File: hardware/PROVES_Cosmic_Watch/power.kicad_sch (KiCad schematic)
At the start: 19 parts, among them J1 USB_B_Micro, J4 Conn_Coaxial, U3 LT3461ES6-TRPBF

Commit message: Updates
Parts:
- removed FB1: 2.5kohm, symbol Device:FerriteBead
- removed J4: Conn_Coaxial, symbol Connector:Conn_Coaxial
- added J2: Conn_01x02, symbol Connector_Generic:Conn_01x02
- added L2: BLM18BD252SN1D, BLM18BD252SN1D:L0603, symbol BLM18BD252SN1D:BLM18BD252SN1D
- J1: footprint (none) -> MOLEX MicroUSB:MICRO-USB-SMD_5P-P0.65-H-F_105164-0001
- U2: renamed from U3; footprint (none) -> LT3461:TSOT-23_S6_LIT
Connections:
- net V_Bias: now also L2.1
- net V_Out: now also L2.2
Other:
- note added: "Power from Payload Computer"
- note removed: "From the Payload Computer"
- note removed: "LT3461"

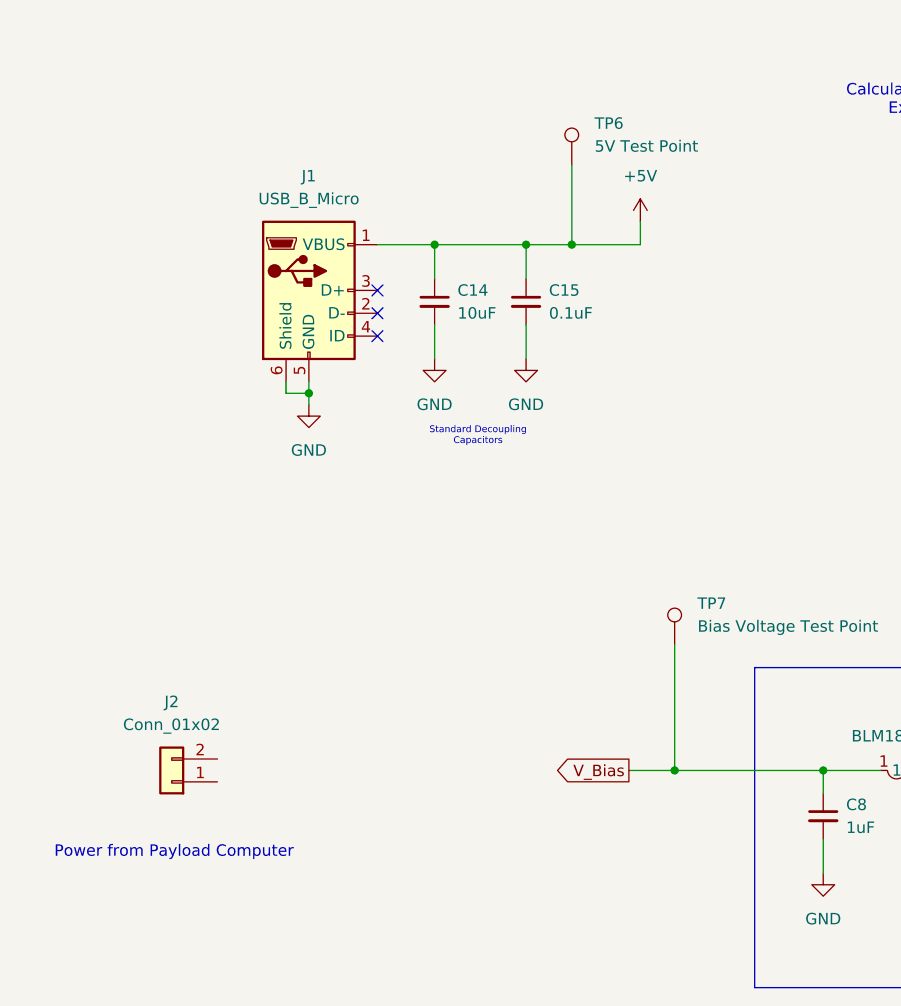
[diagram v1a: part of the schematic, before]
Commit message: Added Footprints and Started Layout
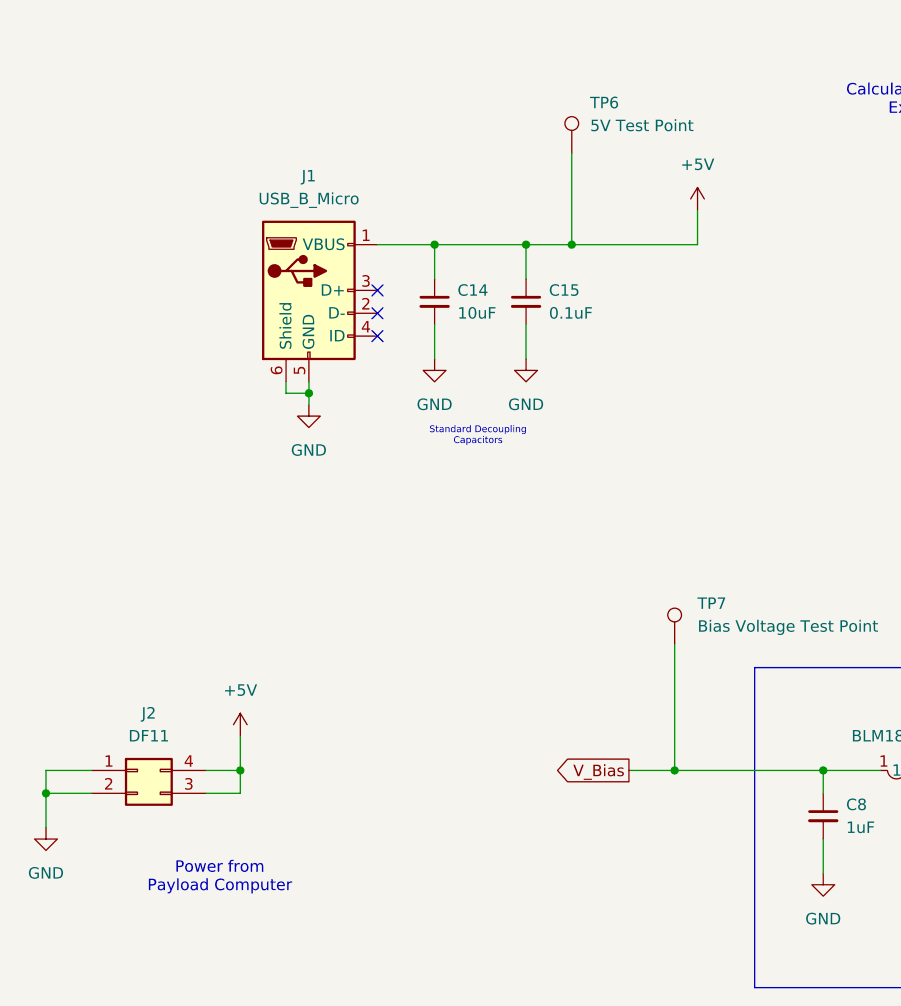
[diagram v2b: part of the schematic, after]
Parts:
- removed J2: Conn_01x02, symbol Connector_Generic:Conn_01x02
- added J2: DF11, DF11-4DP-2DSA:CONN-TH_DF11-4DP-2DSA-08, symbol Connector_Generic:Conn_02x02_Counter_Clockwise
- C14, C15, C16, C5, C6, C8, C9: footprint (none) -> Capacitor_SMD:C_0805_2012Metric
- L1: footprint (none) -> LQH32CN470K23:L1210
- R10, R11, R15: footprint (none) -> Resistor_SMD:R_0805_2012Metric
- TP6, TP7, TP8, TP9: footprint (none) -> TestPoint:TestPoint_Keystone_5000-5004_Miniature
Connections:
- net +5V: now also J2.3 (Pin_3), J2.4 (Pin_4)
- net GND: now also J2.1 (Pin_1), J2.2 (Pin_2)
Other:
- moved on the sheet: TP6

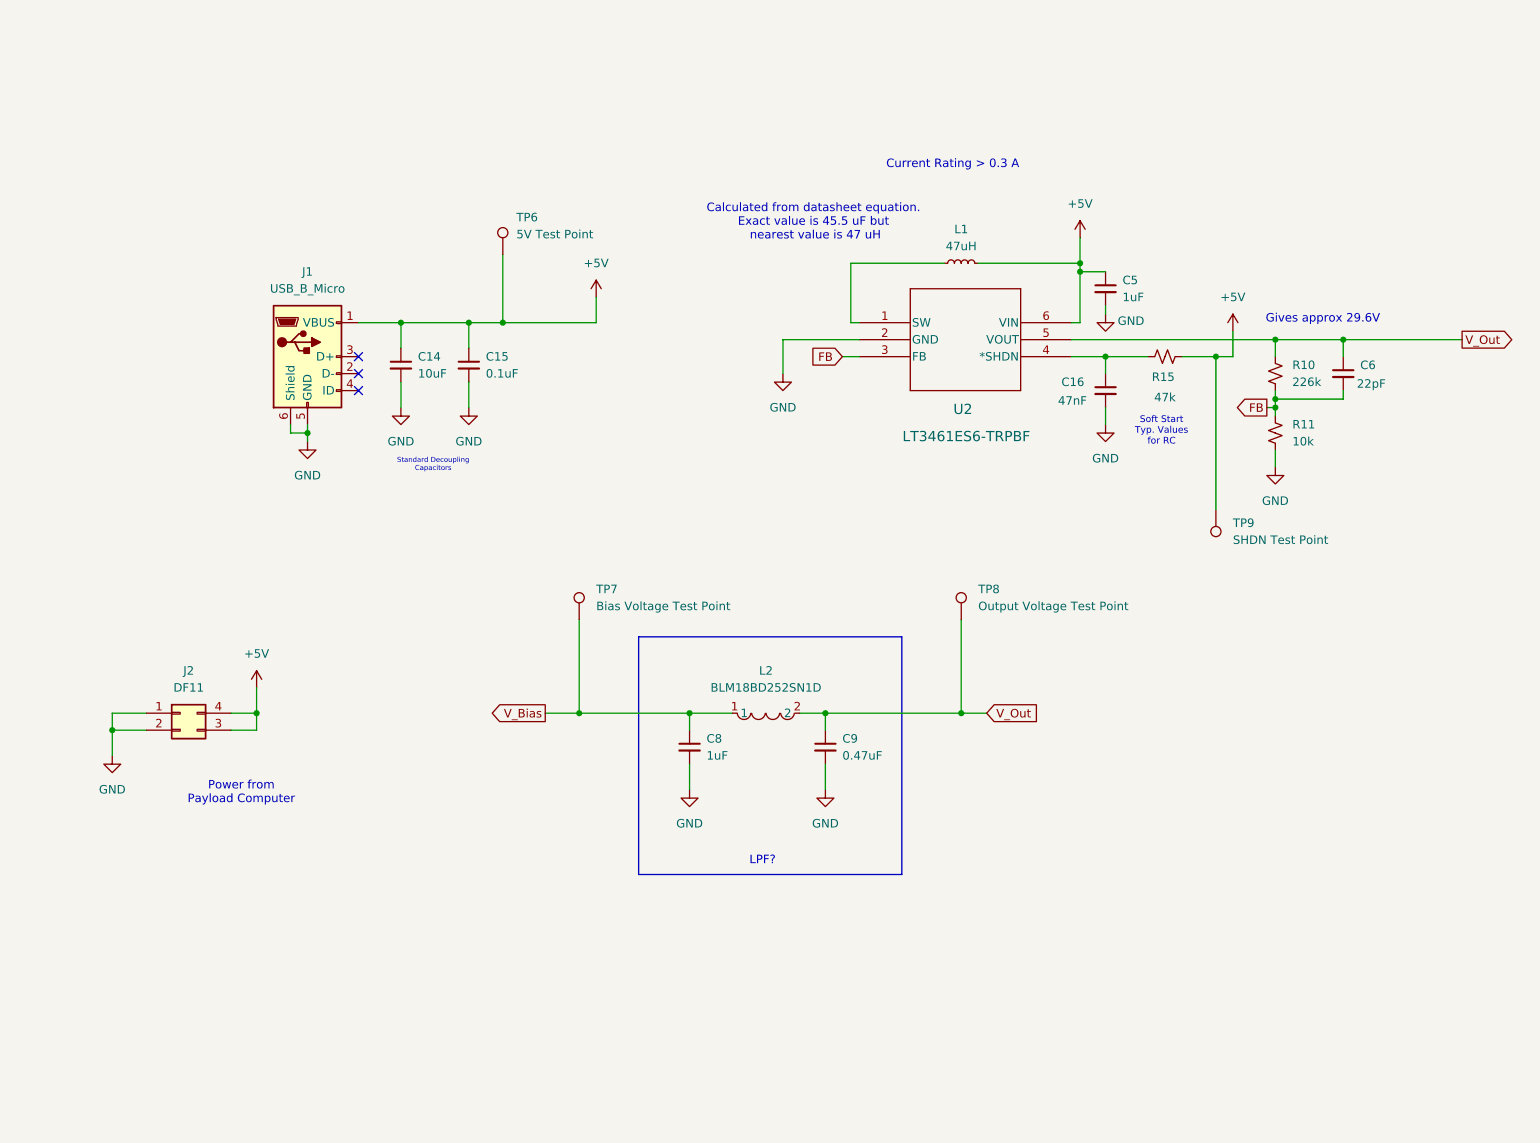
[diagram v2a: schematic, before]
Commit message: Removed LDO
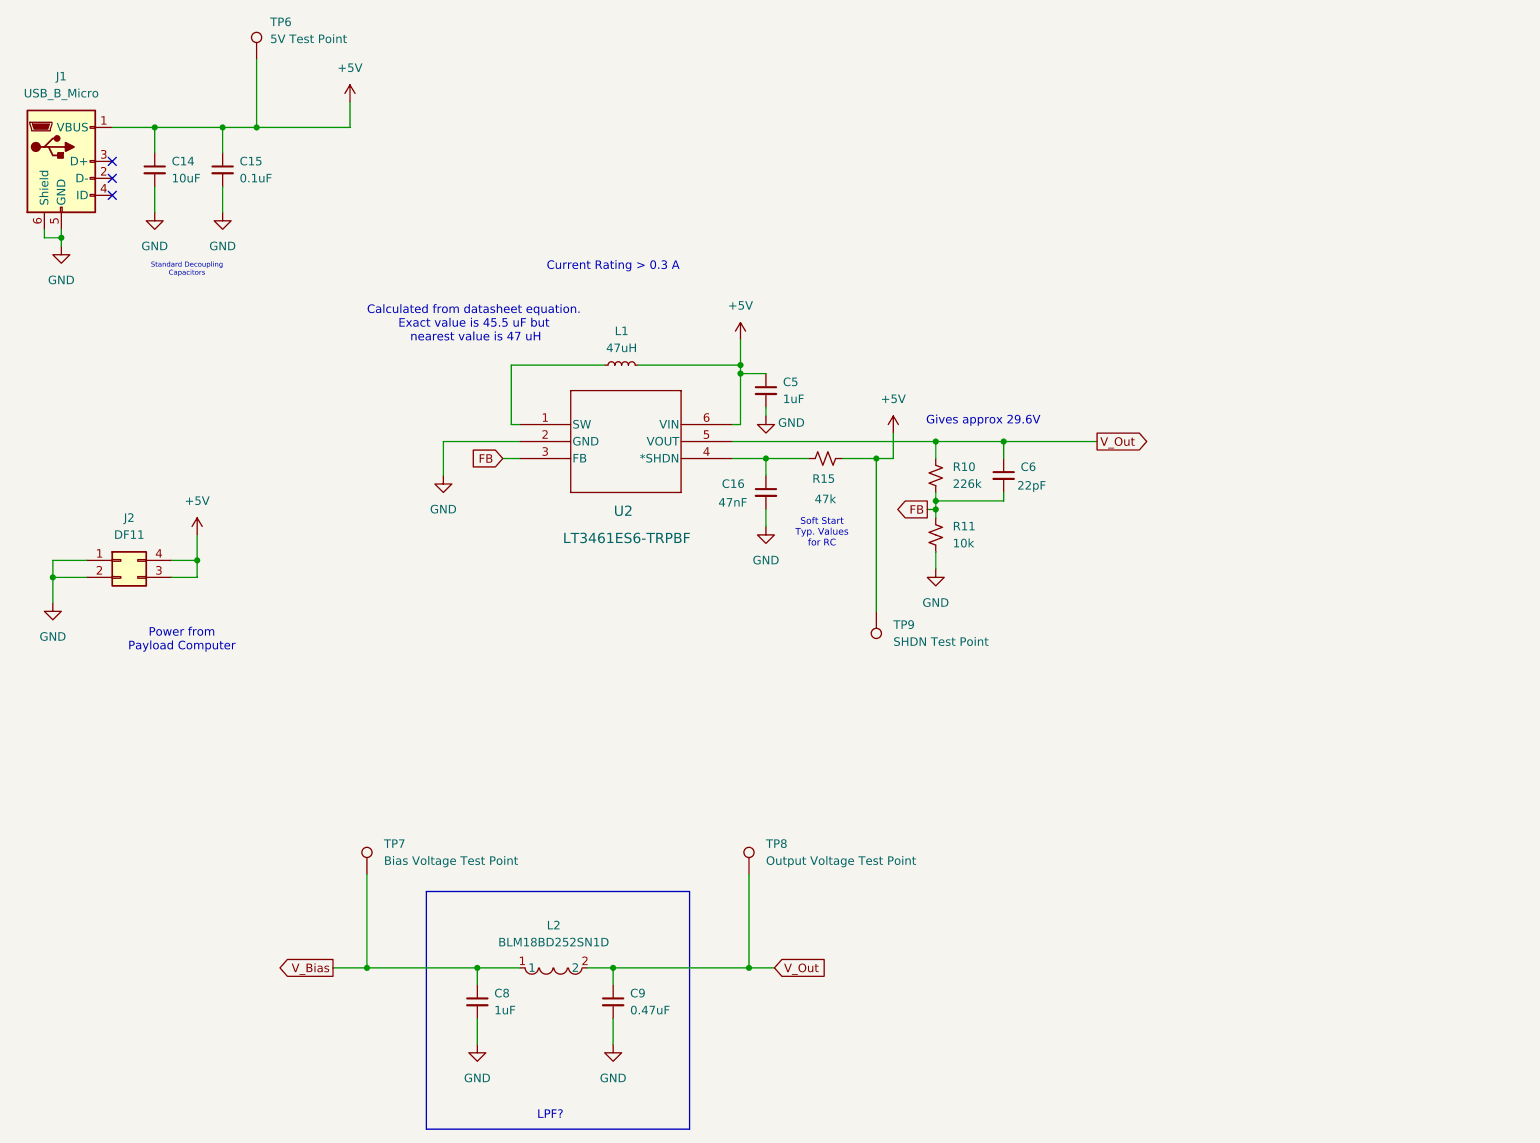
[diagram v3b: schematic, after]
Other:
- moved on the sheet: C14, C15, C16, C5, C6, C8, C9, J1, J2, L1, L2, R10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

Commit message: Layout Updates
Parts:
- TP7: value Bias Voltage Test Point -> FB Test Point
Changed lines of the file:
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@@
 			)
 		)
-		(property "Value" "Bias Voltage Test Point"
+		(property "Value" "FB Test Point"
 			(at 81.28 147.8279 0)
 			(effects

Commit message: Layout Updates
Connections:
- net +5V: no longer TP9.1
- net at C16.1, R15.1, U2.4 (*SHDN): now also TP9.1
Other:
- moved on the sheet: C16, R15, TP9
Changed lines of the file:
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@@
-	)
-	(junction
-		(at 138.43 87.63)
-		(diameter 0)
-		(color 0 0 0 0)
 	)
 	(junction
@@
 	)
 	(junction
-		(at 154.94 87.63)
+		(at 163.83 93.98)
 		(diameter 0)
 		(color 0 0 0 0)
 	)
 	(junction
-		(at 163.83 93.98)
+		(at 140.97 87.63)
 		(diameter 0)
 		(color 0 0 0 0)
@@
 	)
 	(junction
+		(at 133.35 87.63)
+		(diameter 0)
+		(color 0 0 0 0)
+	)
+	(junction
 		(at 163.83 85.09)
 		(diameter 0)
@@
 	(wire
 		(pts
-			(xy 154.94 87.63) (xy 154.94 110.49)
-		)
-		(stroke
-			(width 0)
-			(type default)
-		)
-	)
-	(wire
-		(pts
 			(xy 163.83 93.98) (xy 163.83 95.25)
 		)
@@
 	(wire
 		(pts
+			(xy 133.35 87.63) (xy 133.35 105.41)
+		)
+		(stroke
+			(width 0)
+			(type default)
+		)
+	)
+	(wire
+		(pts
 			(xy 115.57 163.83) (xy 135.89 163.83)
 		)
@@
 	(wire
 		(pts
-			(xy 138.43 87.63) (xy 138.43 90.17)
-		)
-		(stroke
-			(width 0)
-			(type default)
-		)
-	)
-	(wire
-		(pts
-			(xy 138.43 95.25) (xy 138.43 97.79)
-		)
-		(stroke
-			(width 0)
-			(type default)
-		)
-	)
-	(wire
-		(pts
-			(xy 138.43 87.63) (xy 144.78 87.63)
+			(xy 140.97 87.63) (xy 140.97 90.17)
+		)
+		(stroke
+			(width 0)
+			(type default)
+		)
+	)
+	(wire
+		(pts
+			(xy 140.97 95.25) (xy 140.97 97.79)
+		)
+		(stroke
+			(width 0)
+			(type default)
+		)
+	)
+	(wire
+		(pts
+			(xy 140.97 87.63) (xy 147.32 87.63)
 		)
 		(stroke
@@
 	(wire
 		(pts
-			(xy 154.94 87.63) (xy 157.48 87.63)
-		)
-		(stroke
-			(width 0)
-			(type default)
-		)
-	)
-	(wire
-		(pts
-			(xy 149.86 87.63) (xy 154.94 87.63)
+			(xy 133.35 87.63) (xy 140.97 87.63)
+		)
+		(stroke
+			(width 0)
+			(type default)
+		)
+	)
+	(wire
+		(pts
+			(xy 152.4 87.63) (xy 160.02 87.63)
 		)
 		(stroke
@@
 	(wire
 		(pts
-			(xy 157.48 87.63) (xy 157.48 83.82)
+			(xy 160.02 87.63) (xy 160.02 83.82)
 		)
 		(stroke
@@
 		(pts
 			(xy 119.38 73.66) (xy 134.62 73.66)
-		)
-		(stroke
-			(width 0)
-			(type default)
-		)
-	)
-	(wire
-		(pts
-			(xy 133.35 87.63) (xy 138.43 87.63)
 		)
 		(stroke
@@
 	(symbol
 		(lib_id "Connector:TestPoint")
-		(at 154.94 110.49 180)
+		(at 133.35 105.41 180)
 		(unit 1)
 		(exclude_from_sim no)
@@
 		(fields_autoplaced yes)
 		(property "Reference" "TP9"
-			(at 157.48 112.5219 0)
+			(at 135.89 107.4419 0)
 			(effects
 				(font
@@
 		)
 		(property "Value" "SHDN Test Point"
-			(at 157.48 115.0619 0)
+			(at 135.89 109.9819 0)
 			(effects
 				(font
@@
 		)
 		(property "Footprint" "TestPoint:TestPoint_Keystone_5000-5004_Miniature"
-			(at 149.86 110.49 0)
+			(at 128.27 105.41 0)
 			(effects
 				(font
@@
 		)
 		(property "Datasheet" "~"
-			(at 149.86 110.49 0)
+			(at 128.27 105.41 0)
 			(effects
 				(font
@@
 		)
 		(property "Description" "test point"
-			(at 154.94 110.49 0)
+			(at 133.35 105.41 0)
 			(effects
 				(font
@@
 	(symbol
 		(lib_id "power:+5V")
-		(at 157.48 83.82 0)
+		(at 160.02 83.82 0)
 		(unit 1)
 		(exclude_from_sim no)
@@
 		(fields_autoplaced yes)
 		(property "Reference" "#PWR032"
-			(at 157.48 87.63 0)
+			(at 160.02 87.63 0)
 			(effects
 				(font
@@
 		)
 		(property "Value" "+5V"
-			(at 157.48 78.74 0)
+			(at 160.02 78.74 0)
 			(effects
 				(font
@@
 		)
 		(property "Footprint" ""
-			(at 157.48 83.82 0)
+			(at 160.02 83.82 0)
 			(effects
 				(font
@@
 		)
 		(property "Datasheet" ""
-			(at 157.48 83.82 0)
+			(at 160.02 83.82 0)
 			(effects
 				(font
@@
 		)
 		(property "Description" "Power symbol creates a global label with name \"+5V\""
-			(at 157.48 83.82 0)
+			(at 160.02 83.82 0)
 			(effects
 				(font
@@
 	(symbol
 		(lib_id "power:GND")
-		(at 138.43 97.79 0)
+		(at 140.97 97.79 0)
 		(unit 1)
 		(exclude_from_sim no)
@@
 		(fields_autoplaced yes)
 		(property "Reference" "#PWR021"
-			(at 138.43 104.14 0)
+			(at 140.97 104.14 0)
 			(effects
 				(font
@@
 		)
 		(property "Value" "GND"
-			(at 138.43 102.87 0)
+			(at 140.97 102.87 0)
 			(effects
 				(font
@@
 		)
 		(property "Footprint" ""
-			(at 138.43 97.79 0)
+			(at 140.97 97.79 0)
 			(effects
 				(font
@@
 		)
 		(property "Datasheet" ""
-			(at 138.43 97.79 0)
+			(at 140.97 97.79 0)
 			(effects
 				(font
@@
 		)
 		(property "Description" "Power symbol creates a global label with name \"GND\" , ground"
-			(at 138.43 97.79 0)
+			(at 140.97 97.79 0)
 			(effects
 				(font
@@
 	(symbol
 		(lib_id "Device:C_Small")
-		(at 138.43 92.71 0)
+		(at 140.97 92.71 0)
 		(unit 1)
 		(exclude_from_sim no)
@@
 		(dnp no)
 		(property "Reference" "C16"
-			(at 131.826 91.44 0)
+			(at 134.366 91.44 0)
 			(effects
 				(font
@@
 		)
 		(property "Value" "47nF"
-			(at 131.318 94.234 0)
+			(at 133.858 94.234 0)
 			(effects
 				(font
@@
 		)
 		(property "Footprint" "Capacitor_SMD:C_0805_2012Metric"
-			(at 138.43 92.71 0)
+			(at 140.97 92.71 0)
 			(effects
 				(font
@@
 		)
 		(property "Datasheet" "~"
-			(at 138.43 92.71 0)
+			(at 140.97 92.71 0)
 			(effects
 				(font
@@
 		)
 		(property "Description" "Unpolarized capacitor, small symbol"
-			(at 138.43 92.71 0)
+			(at 140.97 92.71 0)
 			(effects
 				(font
@@
 	(symbol
 		(lib_id "Device:R_Small_US")
-		(at 147.32 87.63 90)
+		(at 149.86 87.63 90)
 		(unit 1)
 		(exclude_from_sim no)
@@
 		(dnp no)
 		(property "Reference" "R15"
-			(at 147.066 90.678 90)
+			(at 149.606 90.678 90)
 			(effects
 				(font
@@
 		)
 		(property "Value" "47k"
-			(at 147.32 93.726 90)
+			(at 149.86 93.726 90)
 			(effects
 				(font
@@
 		)
 		(property "Footprint" "Resistor_SMD:R_0805_2012Metric"
-			(at 147.32 87.63 0)
+			(at 149.86 87.63 0)
 			(effects
 				(font
@@
 		)
 		(property "Datasheet" "~"
-			(at 147.32 87.63 0)
+			(at 149.86 87.63 0)
 			(effects
 				(font
@@
 		)
 		(property "Description" "Resistor, small US symbol"
-			(at 147.32 87.63 0)
-			(effects
-				(font
+			(at 149.86 87.63 0)
+			(effects
+				(font

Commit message: Layout Updates
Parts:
- removed TP9: SHDN Test Point, TestPoint:TestPoint_Keystone_5000-5004_Miniature, symbol Connector:TestPoint
- TP7: value FB Test Point -> Post FB
- TP8: value Output Voltage Test Point -> V+ Out
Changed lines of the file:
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@@
-	)
-	(junction
-		(at 133.35 87.63)
-		(diameter 0)
-		(color 0 0 0 0)
 	)
 	(junction
@@
 		(pts
 			(xy 163.83 93.98) (xy 163.83 95.25)
-		)
-		(stroke
-			(width 0)
-			(type default)
-		)
-	)
-	(wire
-		(pts
-			(xy 133.35 87.63) (xy 133.35 105.41)
 		)
 		(stroke
@@
 			)
 		)
-		(property "Value" "Output Voltage Test Point"
+		(property "Value" "V+ Out"
 			(at 138.43 147.8279 0)
 			(effects
@@
 	)
 	(symbol
-		(lib_id "Connector:TestPoint")
-		(at 133.35 105.41 180)
-		(unit 1)
-		(exclude_from_sim no)
-		(in_bom yes)
-		(on_board yes)
-		(dnp no)
-		(fields_autoplaced yes)
-		(property "Reference" "TP9"
-			(at 135.89 107.4419 0)
-			(effects
-				(font
-					(size 1.27 1.27)
-				)
-				(justify right)
-			)
-		)
-		(property "Value" "SHDN Test Point"
-			(at 135.89 109.9819 0)
-			(effects
-				(font
-					(size 1.27 1.27)
-				)
-				(justify right)
-			)
-		)
-		(property "Footprint" "TestPoint:TestPoint_Keystone_5000-5004_Miniature"
-			(at 128.27 105.41 0)
-			(effects
-				(font
-					(size 1.27 1.27)
-				)
-				(hide yes)
-			)
-		)
-		(property "Datasheet" "~"
-			(at 128.27 105.41 0)
-			(effects
-				(font
-					(size 1.27 1.27)
-				)
-				(hide yes)
-			)
-		)
-		(property "Description" "test point"
-			(at 133.35 105.41 0)
-			(effects
-				(font
-					(size 1.27 1.27)
-				)
-				(hide yes)
-			)
-		)
-		(pin "1"
-		)
-		(instances
-			(project "Cosmic_Watch"
-				(path "/901a4a81-3d4a-4d59-b0fc-ea1dade1210f/94b942db-2822-486c-90f4-c726bdd9ff86"
-					(reference "TP9")
-					(unit 1)
-				)
-			)
-		)
-	)
-	(symbol
 		(lib_id "power:GND")
 		(at 138.43 81.28 0)
@@
 			)
 		)
-		(property "Value" "FB Test Point"
+		(property "Value" "Post FB"
 			(at 81.28 147.8279 0)
 			(effects

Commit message: Layout Updates
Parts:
- TP6: value 5V Test Point -> 5V
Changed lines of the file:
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@@
 			)
 		)
-		(property "Value" "5V Test Point"
+		(property "Value" "5V"
 			(at 64.262 24.892 0)
 			(effects

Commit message: Updates
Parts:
- removed C14: 10uF, Capacitor_SMD:C_0805_2012Metric, symbol Device:C_Small
- removed C15: 0.1uF, Capacitor_SMD:C_0805_2012Metric, symbol Device:C_Small
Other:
- note removed: "Standard Decoupling Capacitors"
